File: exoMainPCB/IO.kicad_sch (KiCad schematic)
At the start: 0 parts

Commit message: finished IO and added Handheld components
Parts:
- added C10, C11, C16, C17: 22 pF, symbol Device:C
- added C12, C13, C14, C15: 104, symbol Device:C
- added J1, J3: Conn_01x03_Pin, symbol Connector:Conn_01x03_Pin
- added JP1, JP2: SolderJumper_3_Bridged12, symbol Jumper:SolderJumper_3_Bridged12
- added R13, R20: 10k, symbol Device:R
- added R15, R17: 1k, symbol Device:R
- added R16, R18: 120, symbol Device:R
- added U10, U9: SM24CANB-02HTG, SOT23-3_SM24CANB-02HTG_LTF, symbol SM24CANB:SM24CANB-02HTG
- added U3, U8: SN65HVD230D, SN65HVD230:D8, symbol SN65HVD230:SN65HVD230D
- added U5, U6: MCP2515-I/ST, MCP2515-IST:TSSOP20_MC_MCH, symbol MCP2515-IST:MCP2515-I_ST
- added U7: SI8642ED-B-IS, SOIC-16W_SIL, symbol SI8642ED-B-IS:SI8642ED-B-IS
- added Y4, Y5: 16 MHz, symbol Device:Crystal
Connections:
- new net: C13.1, U7.16 (VDD2)
- new net: R20.2, U6.19 (*RESET)
- new net: R20.1, U6.20 (VDD)
- new net: C16.2, U6.8 (OSC2), Y5.2
- new net: C17.2, U6.9 (OSC1), Y5.1
- new net: J1.2 (Pin_2), JP1.1 (A), U3.6 (CANL), U9.3
- new net: JP1.2 (C), R16.2
- new net: R13.1, U5.20 (VDD)
- new net: R13.2, U5.19 (*RESET)
- new net: J1.3 (Pin_3), R16.1, U3.7 (CANH), U9.2
- new net: C11.2, U5.9 (OSC1), Y4.1
- new net: C10.2, U5.8 (OSC2), Y4.2
- new net: J3.3 (Pin_3), R18.1, U10.2, U8.7 (CANH)
- new net: JP2.2 (C), R18.2
- new net: J3.2 (Pin_2), JP2.1 (A), U10.3, U8.6 (CANL)
- new net: C15.1, U8.3 (VCC)
- new net: R17.2, U8.8 (RS)
- new net: C14.2, U7.1 (VDD1)
- new net: R15.2, U3.8 (RS)
- new net: C12.1, U3.3 (VCC)
- new net D_{CS0}: U5.18 (*CS)
- new net D_{CS1}: U6.18 (*CS)
- new net D_{INT0}: U5.13 (*INT)
- new net D_{INT1}: U6.13 (*INT)
- new net D_{SCK0}: U5.14 (SCK)
- new net D_{SCK1}: U6.14 (SCK)
- new net D_{SI0}: U5.16 (SI)
- new net D_{SI1}: U6.16 (SI)
- new net D_{SO0}: U5.17 (SO)
- new net D_{SO1}: U6.17 (SO)
- new net GND: C10.1, C11.1, C16.1, C17.1, U5.10 (VSS), U6.10 (VSS), U7.8 (GND1)
- new net GNDS: C12.2, C13.2, C14.1, C15.2, J1.1 (Pin_1), J3.1 (Pin_1), R15.1, R17.1, U10.1, U3.2 (GND), U7.15 (GND2), U7.2 (GND1), U7.9 (GND2), U8.2 (GND), U9.1
- new net RXD 0A: U5.2 (RXCAN), U7.5 (A3)
- new net RXD 0B: U3.4 (R), U7.12 (B3)
- new net RXD 1A: U6.2 (RXCAN), U7.6 (A4)
- new net RXD 1B: U7.11 (B4), U8.4 (R)
- new net TXD 0A: U5.1 (TXCAN), U7.3 (A1)
- new net TXD 0B: U3.1 (D), U7.14 (B1)
- new net TXD 1A: U6.1 (TXCAN), U7.4 (A2)
- new net TXD 1B: U7.13 (B2), U8.1 (D)
- no-connect marks 0 -> 2

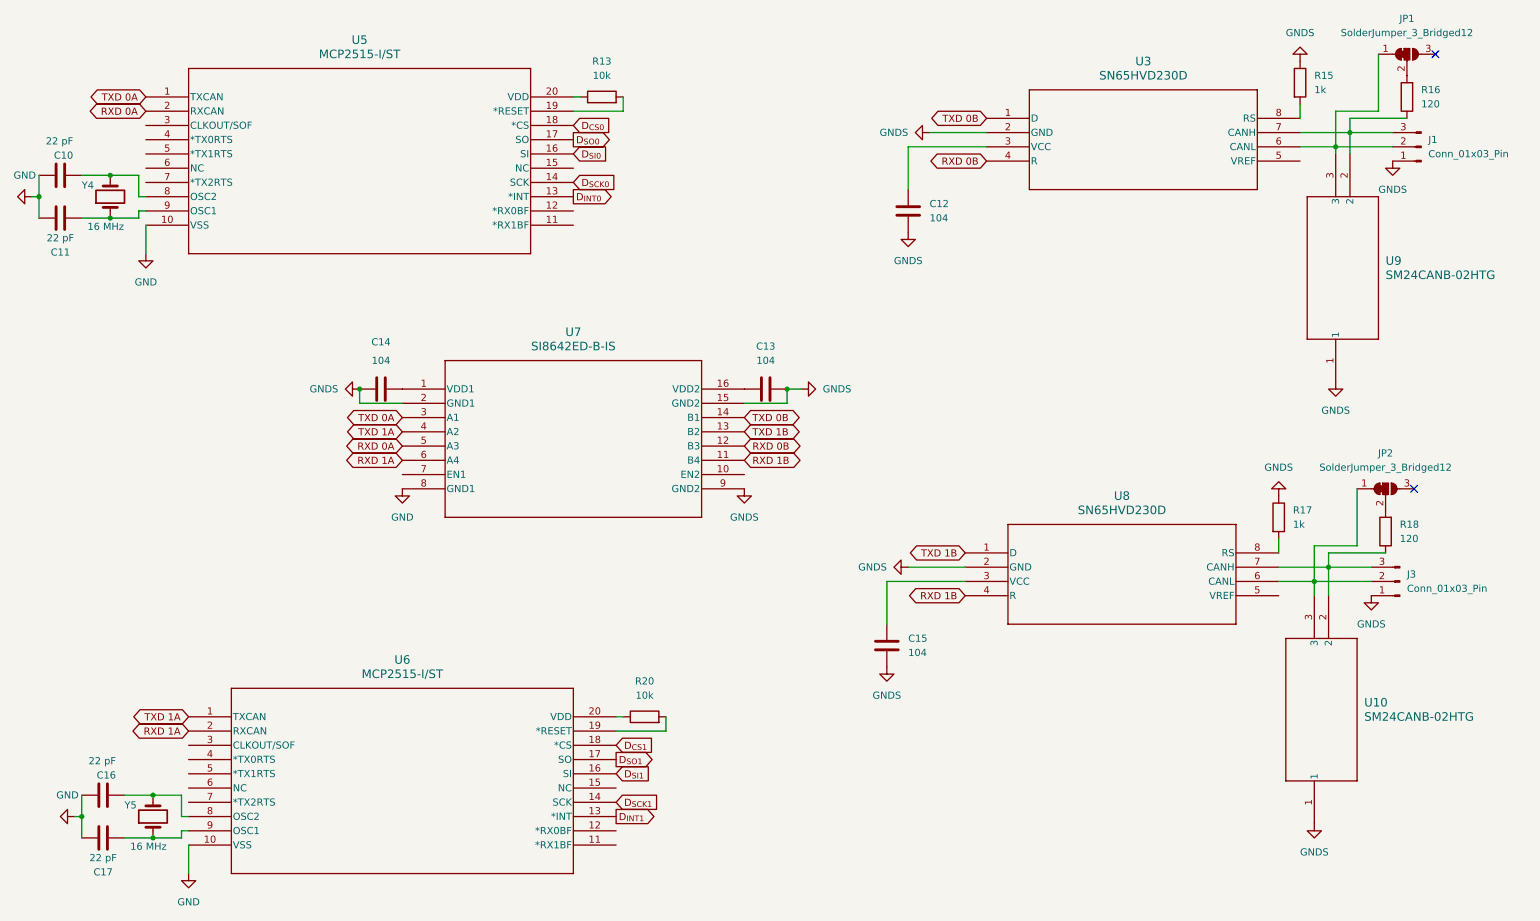
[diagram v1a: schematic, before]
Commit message: changed all resistors to US, updated IO, finished Handheld
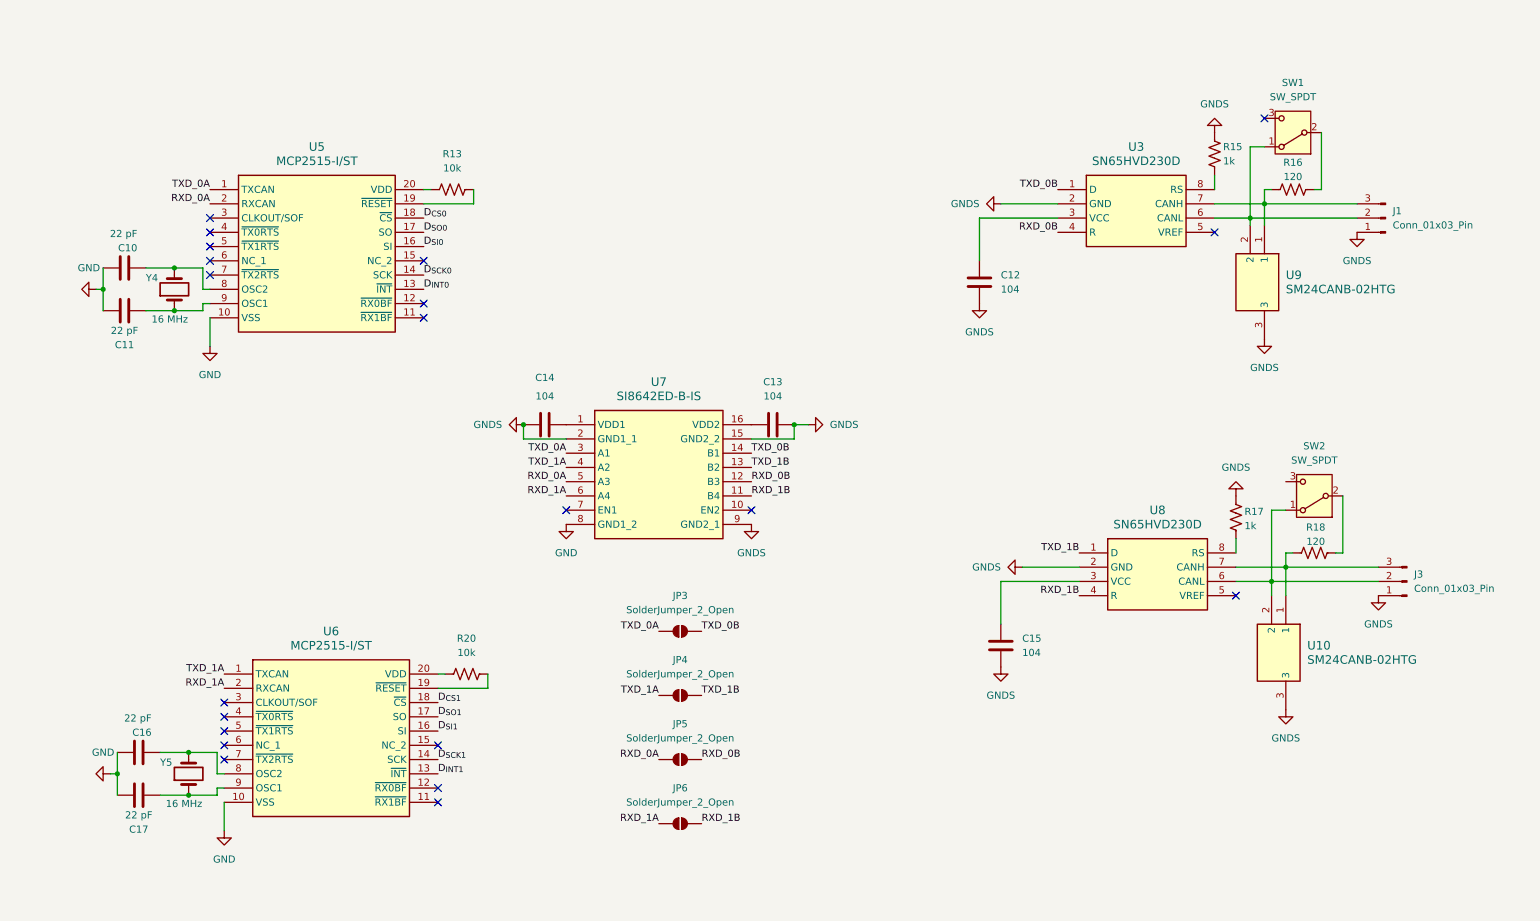
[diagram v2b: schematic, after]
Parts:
- removed JP1, JP2: SolderJumper_3_Bridged12, symbol Jumper:SolderJumper_3_Bridged12
- added JP3, JP4, JP5, JP6: SolderJumper_2_Open, symbol Jumper:SolderJumper_2_Open
- added SW1, SW2: SW_SPDT, symbol Switch:SW_SPDT
- R13, R15, R16, R17, R18, R20: symbol Device:R -> Device:R_US
- U10, U9: footprint SOT23-3_SM24CANB-02HTG_LTF -> SM24CANB02HTG; Arrow Part Number (none) -> SM24CANB-02HTG; Arrow Price/Stock (none) -> https://www.arrow.com/en/products/sm24canb-02htg/littelfuse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; Height (none) -> 1.12; Manufacturer_Name (none) -> LITTELFUSE; Manufacturer_Part_Number (none) -> SM24CANB-02HTG; Mouser Part Number (none) -> 576-SM24CANB-02HTG; Mouser Price/Stock (none) -> https://www.mouser.co.uk/ProductDetail/Littelfuse/SM24CANB-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
- U3, U8: footprint SN65HVD230:D8 -> SOIC127P600X175-8N; Arrow Part Number (none) -> SN65HVD230D; Arrow Price/Stock (none) -> https://www.arrow.com/en/products/sn65hvd230d/texas-instrum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; Height (none) -> 1.75; Manufacturer_Name (none) -> Texas Instruments; Manufacturer_Part_Number (none) -> SN65HVD230D; Mouser Part Number (none) -> 595-SN65HVD230D; Mouser Price/Stock (none) -> https://www.mouser.co.uk/ProductDetail/Texas-Instruments/SN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
- U5, U6: footprint MCP2515-IST:TSSOP20_MC_MCH -> SOP65P640X120-20N; Arrow Part Number (none) -> MCP2515-I/ST; Arrow Price/Stock (none) -> https://www.arrow.com/en/products/mcp2515-ist/microchip-tec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; Height (none) -> 1.2; Manufacturer_Name (none) -> Microchip; Manufacturer_Part_Number (none) -> MCP2515-I/ST; Mouser Part Number (none) -> 579-MCP2515-I/ST; Mouser Price/Stock (none) -> https://www.mouser.co.uk/ProductDetail/Microchip-Technology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
- U7: footprint SOIC-16W_SIL -> SOIC127P1030X265-16N; symbol SI8642ED-B-IS:SI8642ED-B-IS -> SI8642ED-B-IS:Si8642ED-B-IS; Arrow Part Number (none) -> SI8642ED-B-IS; Arrow Price/Stock (none) -> https://www.arrow.com/en/products/si8642ed-b-is/silicon-lab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; Height (none) -> 2.65; Manufacturer_Name (none) -> Silicon Labs; Manufacturer_Part_Number (none) -> Si8642ED-B-IS; Mouser Part Number (none) -> 634-SI8642ED-B-IS; Mouser Price/Stock (none) -> https://www.mouser.com/Search/Refine.aspx?Keyword=634-SI864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
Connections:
- net GNDS: now also U10.3, U9.3; no longer U10.1, U9.1
- net at J1.2 (Pin_2), U3.6 (CANL): now also U9.2, SW1.1 (A); no longer U9.3
- net at R16.2: now also J1.3 (Pin_3), U3.7 (CANH), U9.1
- net at J3.3 (Pin_3), U8.7 (CANH): now also R18.2, U10.1; no longer R18.1, U10.2
- net at J3.2 (Pin_2), U8.6 (CANL): now also U10.2, SW2.1 (A); no longer U10.3
- net RXD 0A renamed RXD_0A
- net RXD_0A: now also JP5.1 (A)
- net RXD 0B renamed RXD_0B
- net RXD_0B: now also JP5.2 (B)
- net RXD 1A renamed RXD_1A
- net RXD_1A: now also JP6.1 (A)
- net RXD 1B renamed RXD_1B
- net RXD_1B: now also JP6.2 (B)
- net TXD 0A renamed TXD_0A
- net TXD_0A: now also JP3.1 (A)
- net TXD 0B renamed TXD_0B
- net TXD_0B: now also JP3.2 (B)
- net TXD 1A renamed TXD_1A
- net TXD_1A: now also JP4.1 (A)
- net TXD 1B renamed TXD_1B
- net TXD_1B: now also JP4.2 (B)
- new net: R18.1, SW2.2 (B)
- new net: R16.1, SW1.2 (B)
- no-connect marks 2 -> 21
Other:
- moved on the sheet: C10, C11, C12, C13, C14, C15, C16, C17, J1, J3, Y4, Y5
